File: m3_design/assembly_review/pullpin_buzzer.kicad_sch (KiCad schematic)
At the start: 10 parts, among them J123 PULL-PIN 1x2, Q123 AO3400A

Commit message: Make R2 orderable: stocked drop-ins, JLC placement corrections, ordering guide
- Stock (JLC assembly API): U8 AP63200 -> AP63300WU-7 (same TSOT26 pinout,
  VFB, fsw), L3 -> SRP5030T-6R8M (same body/land, AP63300 Table 1), C77
  100p -> 47p (Table 1), C84 25SVPF330M -> 35SVPK330M (same OS-CON F12).
  Every BOM line now has JLC stock for 5 boards except U6 SAM-M10Q
  (consign / Global Sourcing; DigiKey has stock).
- tools/jlc_orient.py matches each footprint pad-by-pad to the LCSC/EasyEDA
  footprint of its LCSC code; export_fab.py applies the rotation/offset.
  Without it U7, U8, U10, U11, U12, U13, D121 and LED2 would be rotated.
- tools/jlc_stock.py: repeatable stock check; fab/stock_check.json.
- JLC_Assembly field: U6 consign note, J2/J123 hand-cut from one 1x40 strip.
- docs/ORDERING.md: PCB options, PCBA, preview checklist, off-board parts.

DRC 0 / unconnected 0 / parity 0 / ERC 0, audit OK; contract OK;
tests 173/112/12 pass; sim 135 PASS.

Co-Authored-By: Claude Opus 5.5 (1M context) <noreply@anthropic.com>
Claude-Session: https://claude.ai/code/session_01DdkfTxR7SVyv9xZNmPk9vB
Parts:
- J123: JLC_Assembly (none) -> Hand: cut 1x2 from the same 1x40 strip C2337 as J2
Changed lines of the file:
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@@
+				(font
+					(size 1.27 1.27))))
+		(property "JLC_Assembly" "Hand: cut 1x2 from the same 1x40 strip C2337 as J2"
+			(at 40.64 50.8 0)
+			(hide yes)
+			(effects
 				(font
 					(size 1.27 1.27))))

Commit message: Full PCBA: stocked J2/J123 headers, THT parts in the CPL with orientation corrections
- J2 -> PZ254V-11-06P (C492405), J123 -> PZ254V-11-02P (C492401); JLC cannot
  cut the former 1x40 strip.
- export_fab.py writes through-hole parts to the CPL (JLC THT assembly) and
  marks them 'THT (JLC THT assembly)'.
- jlc_corrections.json keyed by LCSC code + footprint (J1 and J9/J120/J121
  share C2915641 with two footprint variants); THT pad data added.
- ORDERING.md: full PCBA; U6 via JLC Global Sourcing or consignment.

DRC 0 / unconnected 0 / parity 0 / ERC 0, audit OK; contract OK; tests pass.

Co-Authored-By: Claude Opus 5.5 (1M context) <noreply@anthropic.com>
Claude-Session: https://claude.ai/code/session_01DdkfTxR7SVyv9xZNmPk9vB
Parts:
- J123: JLC_Assembly Hand: cut 1x2 from the same 1x40 strip C2337 as J2 -> (none); LCSC C2337 -> C492401; LCSC Part (none) -> C492401; Manufacturer (none) -> XFCN; Manufacturer Part (none) -> PZ254V-11-02P
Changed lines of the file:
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@@
 				(font
 					(size 1.27 1.27))))
-		(property "LCSC" "C2337"
+		(property "LCSC" "C492401"
 			(at 40.64 50.8 0)
 			(hide yes)
@@
 				(font
 					(size 1.27 1.27))))
-		(property "JLC_Assembly" "Hand: cut 1x2 from the same 1x40 strip C2337 as J2"
+		(property "LCSC Part" "C492401"
 			(at 40.64 50.8 0)
 			(hide yes)
+			(effects
+				(font
+					(size 1.27 1.27))))
+		(property "Manufacturer" "XFCN"
+			(at 40.64 50.8 0)
+			(hide yes)
+			(effects
+				(font
+					(size 1.27 1.27))))
+		(property "Manufacturer Part" "PZ254V-11-02P"
+			(at 40.64 50.8 0)
+			(hide yes)

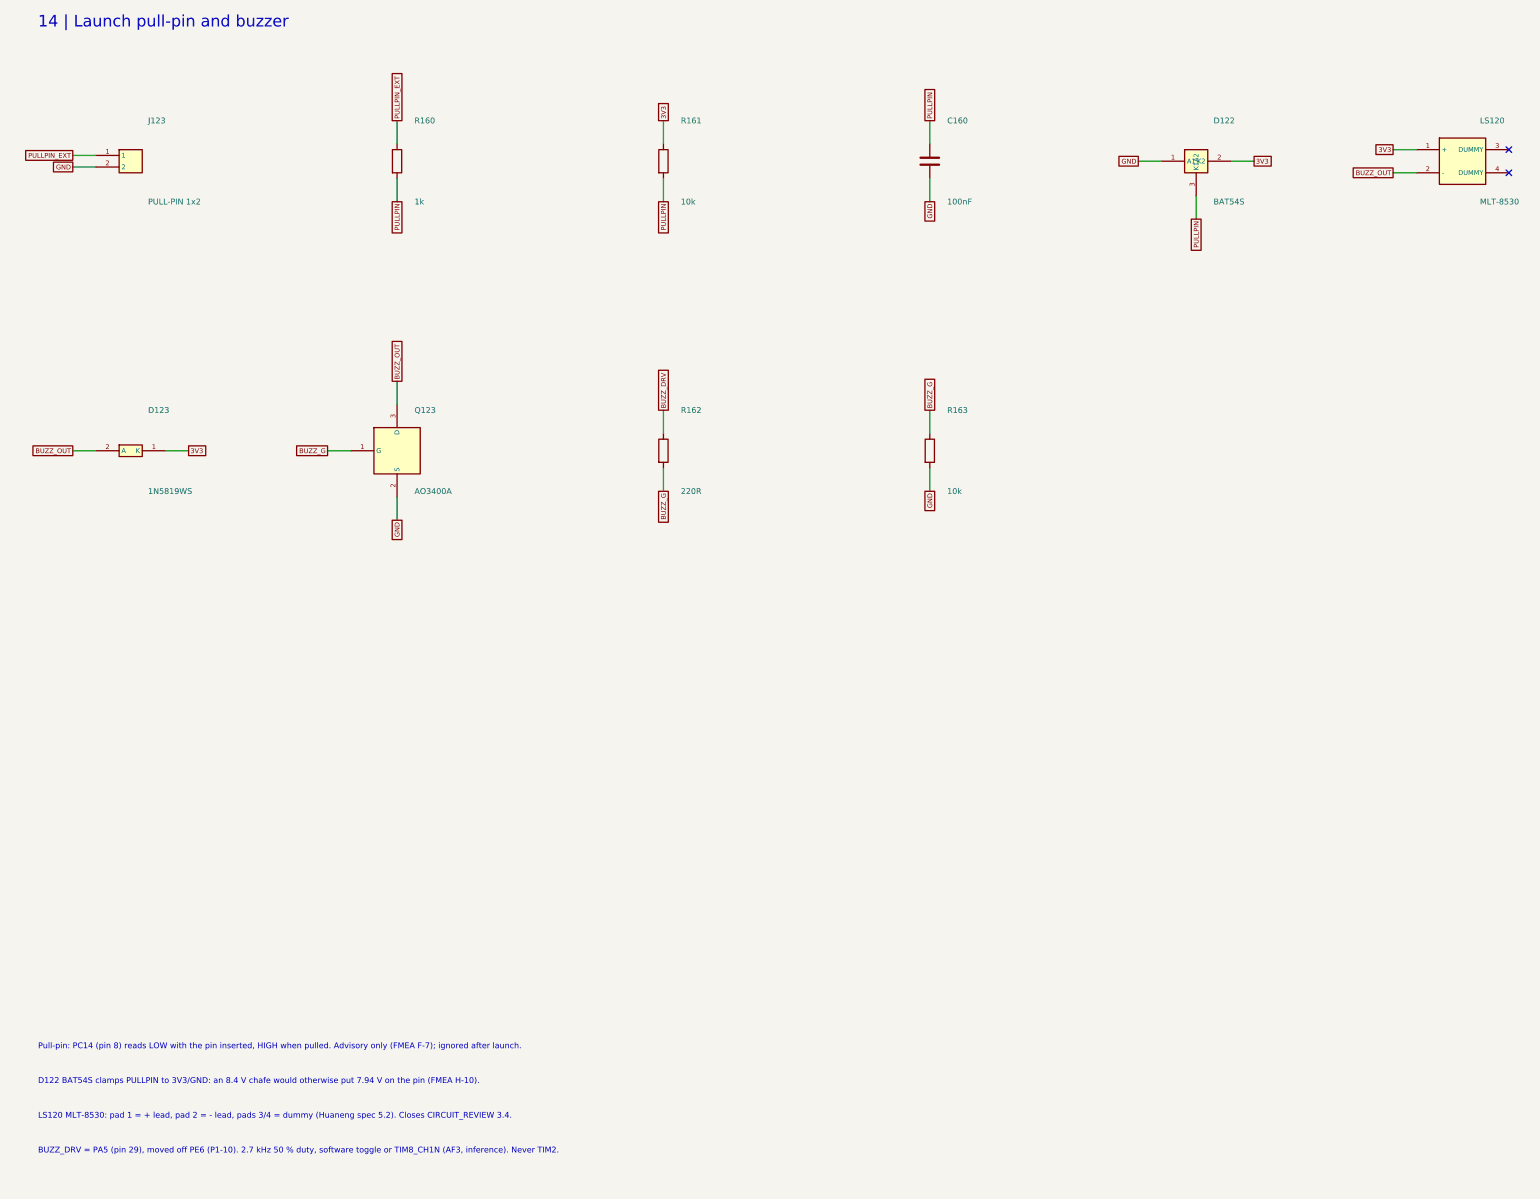
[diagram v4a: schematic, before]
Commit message: M3-ASSY-R4: R3 validation fixes, new IMU, fault-tolerant pyro sensing
The board, schematic sheets and footprint library are generated from
R3 (533af8e) by m3_design/r4_build.sh (r4_lib.py, r4_sch.py,
r4_pcb.py). docs/REQUIREMENTS.md states what the board must do;
docs/M3_R4.md records every change, the thirteen evaluation passes
(twelve independent reviews) and the accepted deviations.

- IMU: ST LSM6DSV320X (16 g and 320 g, 4000 dps)
- Pyro: black ARM and orange igniter terminals, eight pyro spacing
  rules in m3.kicad_dru, sense dividers of 2 x 5.1k over 2 x 2k in
  parallel, 4.7k at each ADC pin (R168-R172)
- Pull-pin on a JST PH connector; JLC tooling holes
- Fab: Standard PCBA, 84 BOM lines, 205 placed parts, $80.12 per board
  at five boards (tools/jlc_cost.py); placement rotations verified
- Gate: tools/check.sh DRC 0, unconnected 0, schematic parity 0, ERC 0,
  audit OK; m3_design/check_actuators.py OK

Nothing has been built or measured, and there is no R4 firmware. The
open owner decisions and the bench tests are listed in STATUS.md.

Co-Authored-By: Claude Opus 5.5 <noreply@anthropic.com>
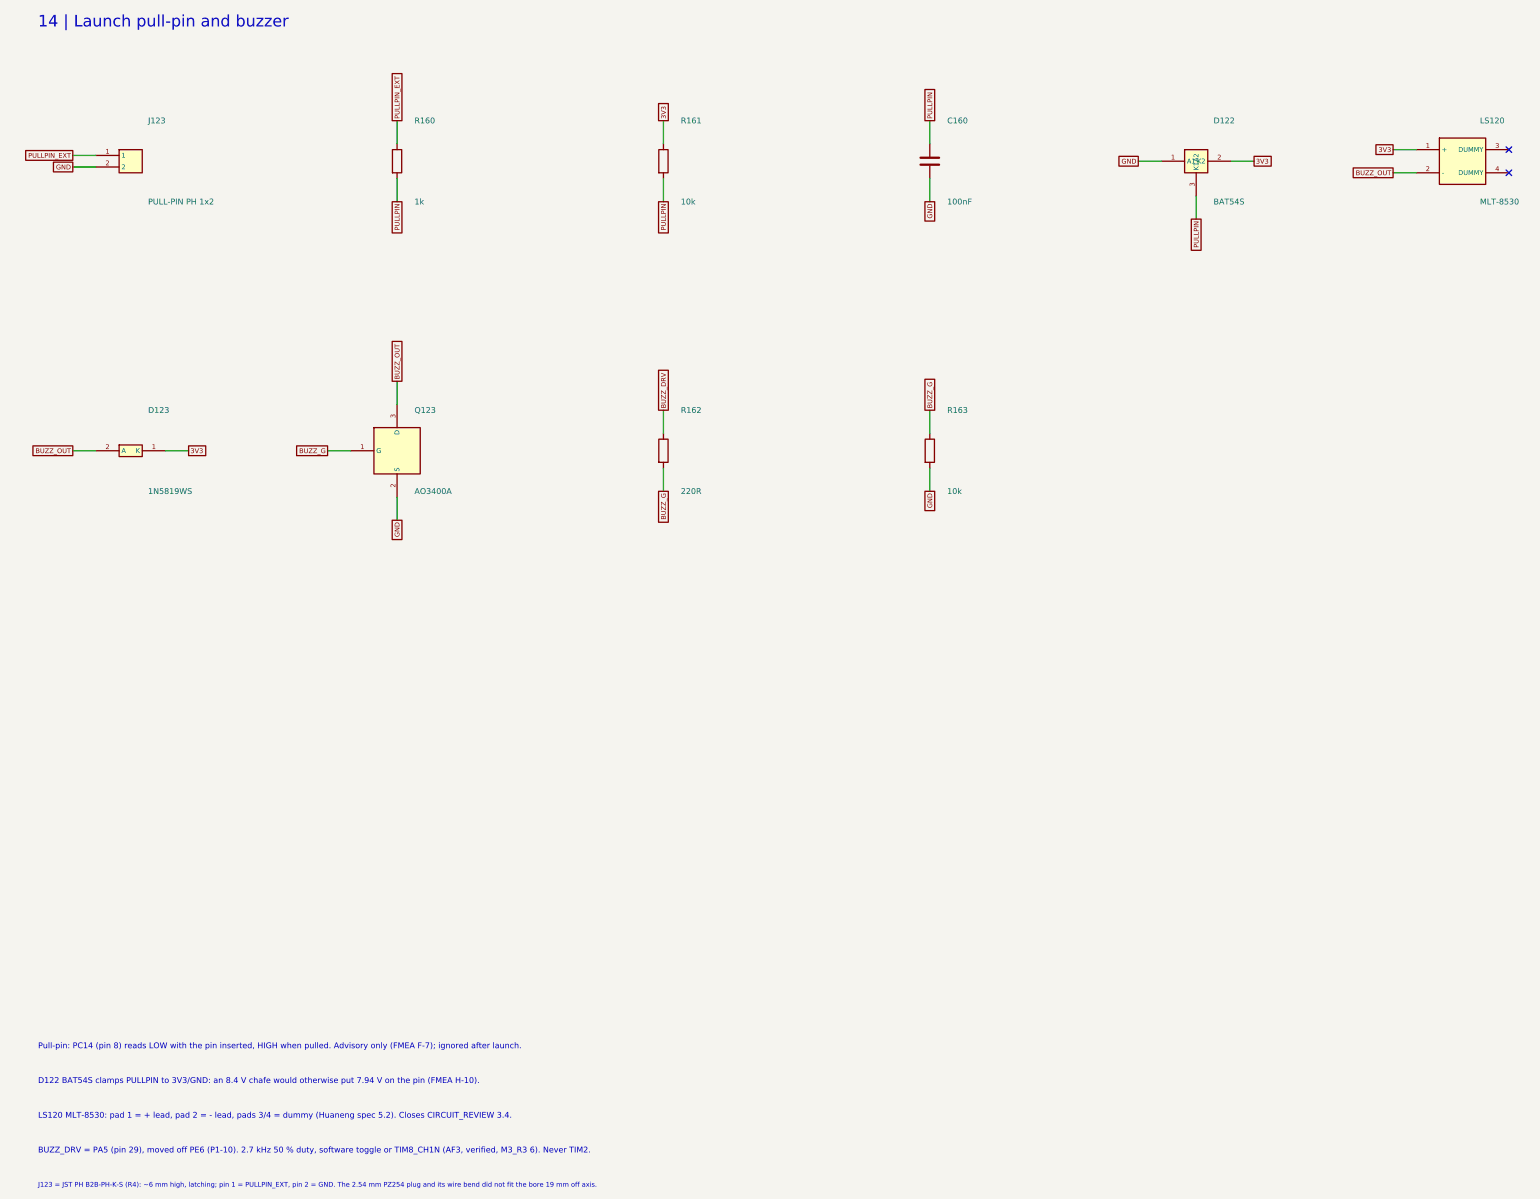
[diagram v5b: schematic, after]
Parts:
- J123: value PULL-PIN 1x2 -> PULL-PIN PH 1x2; footprint rocket:M3_PULLPIN_1x2 -> rocket:M3_JST_PH_B2B_2P; LCSC C492401 -> C131337; LCSC Part C492401 -> C131337; Manufacturer XFCN -> JST; Manufacturer Part PZ254V-11-02P -> B2B-PH-K-S(LF)(SN)
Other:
- note added: "BUZZ_DRV = PA5 (pin 29), moved off PE6 (P1-10). 2.7 kHz 50 % duty, software toggle or TIM8_CH1N (AF3, verified, M3_R3 6). Never TIM2."
- note added: "J123 = JST PH B2B-PH-K-S (R4): ~6 mm high, latching; pin 1 = PULLPIN_EXT, pin 2 = GND. The 2.54 mm PZ254 plug and its wire bend did not fit the bore 19 mm off axis."
- note removed: "BUZZ_DRV = PA5 (pin 29), moved off PE6 (P1-10). 2.7 kHz 50 % duty, software toggle or TIM8_CH1N (AF3, inference). Never TIM2."
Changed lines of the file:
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@@
 		(title "14 | Launch pull-pin and buzzer")
 		(date "2026-09-25")
-		(rev "M3-ASSY-R3")
+		(rev "M3-ASSY-R4")
 		(company "Single-board M3 candidate; actuator merge, not bench-verified"))
 	(symbol
@@
 					(size 1.27 1.27))
 				(justify left)))
-		(property "Value" "PULL-PIN 1x2"
+		(property "Value" "PULL-PIN PH 1x2"
 			(at 44.45 59.69 0)
 			(effects
@@
 					(size 1.27 1.27))
 				(justify left)))
-		(property "Footprint" "rocket:M3_PULLPIN_1x2"
+		(property "Footprint" "rocket:M3_JST_PH_B2B_2P"
 			(at 40.64 50.8 0)
 			(hide yes)
@@
 				(font
 					(size 1.27 1.27))))
-		(property "LCSC" "C492401"
+		(property "LCSC" "C131337"
 			(at 40.64 50.8 0)
 			(hide yes)
@@
 				(font
 					(size 1.27 1.27))))
-		(property "LCSC Part" "C492401"
+		(property "LCSC Part" "C131337"
 			(at 40.64 50.8 0)
 			(hide yes)
@@
 				(font
 					(size 1.27 1.27))))
-		(property "Manufacturer" "XFCN"
+		(property "Manufacturer" "JST"
 			(at 40.64 50.8 0)
 			(hide yes)
@@
 				(font
 					(size 1.27 1.27))))
-		(property "Manufacturer Part" "PZ254V-11-02P"
+		(property "Manufacturer Part" "B2B-PH-K-S(LF)(SN)"
 			(at 40.64 50.8 0)
 			(hide yes)
@@
 			(justify left))
 )
-	(text "BUZZ_DRV = PA5 (pin 29), moved off PE6 (P1-10). 2.7 kHz 50 % duty, software toggle or TIM8_CH1N (AF3, inference). Never TIM2."
+	(text "BUZZ_DRV = PA5 (pin 29), moved off PE6 (P1-10). 2.7 kHz 50 % duty, software toggle or TIM8_CH1N (AF3, verified, M3_R3 6). Never TIM2."
 		(at 20.32 267.86 0)
 		(effects
@@
 			(justify left))
 )
+	(text "J123 = JST PH B2B-PH-K-S (R4): ~6 mm high, latching; pin 1 = PULLPIN_EXT, pin 2 = GND. The 2.54 mm PZ254 plug and its wire bend did not fit the bore 19 mm off axis."
+		(at 20.32 275.48 0)
+		(effects
+			(font
+				(size 1.05 1.05))
+			(justify left))
+)
